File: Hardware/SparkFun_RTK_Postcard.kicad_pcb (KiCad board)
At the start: 4 copper layers, 43.2 x 43.2 mm, 151 parts, among them J1 USB_C_Receptacle, J11 1x10, J2 SMA_Edge, J4 Qwiic_RA, J5 1x09, J6 U.FL, J7 Qwiic_RA, J8 JST_Locking_4, Q1 MBT3904DW1, SW4 Reset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

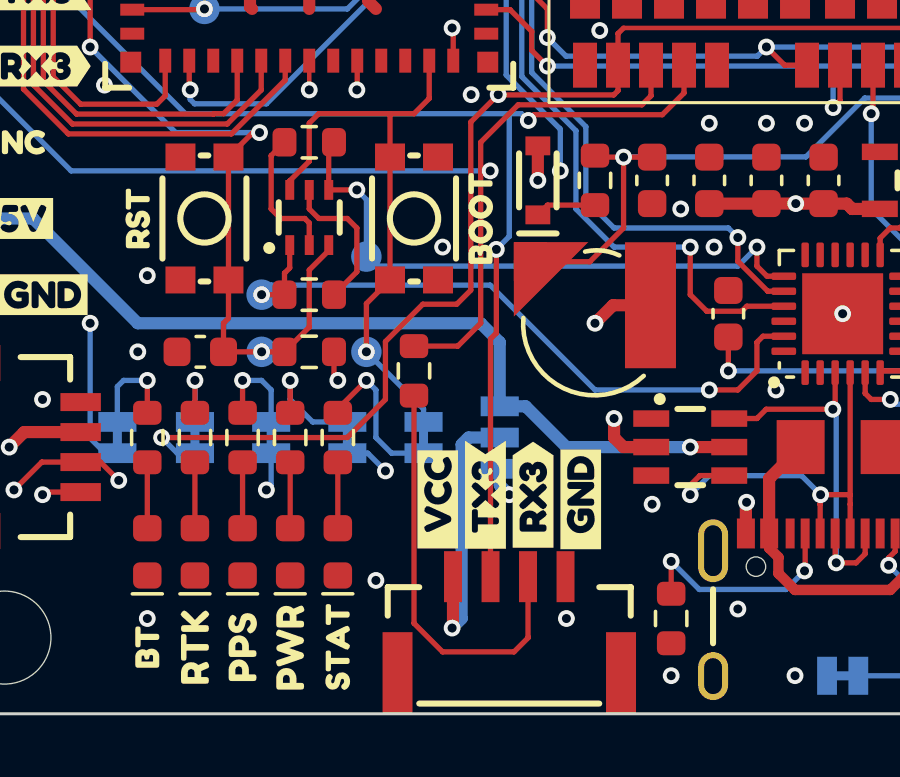
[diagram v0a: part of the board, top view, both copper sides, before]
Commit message: Update to v9 and current libraries.
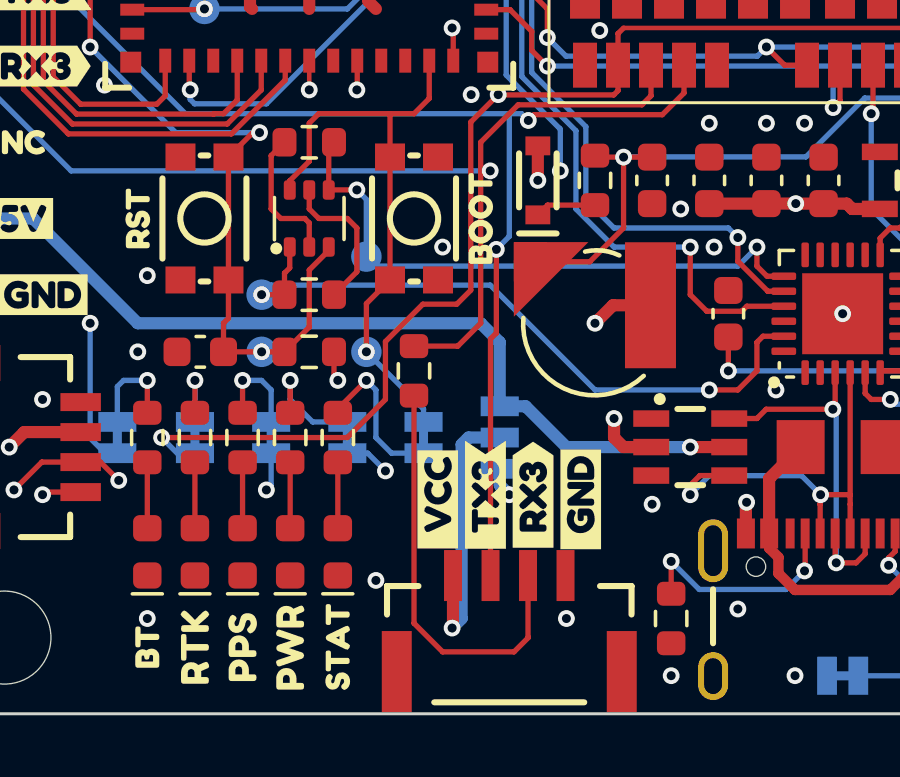
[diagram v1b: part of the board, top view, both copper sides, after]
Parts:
- removed Q1: MBT3904DW1, SparkFun-Semiconductor-Standard:SOT-323
- added Q2: MBT3904DW1, SparkFun-Semiconductor-Standard:SOT-363_SC-70-6, F.Cu at (148.0, 101.0)
- BT1: value 6.8mm_ML414H -> ML414H
- J11: footprint SparkFun-Connector:1x10 -> SparkFun-Connector:1x10_P2.54mm
- J2: footprint SparkFun-Connector:SMA_Edge -> SparkFun-Connector:SMA_Edge_8mm
- J4, J7: footprint SparkFun-Connector:JST_SMD_1.0mm-4_RA -> SparkFun-Connector:JST_1x04_P1.0mm_Horizontal_SMD
- J5: footprint SparkFun-Connector:1x09 -> SparkFun-Connector:1x09_P2.54mm
- J8: footprint SparkFun-Connector:JST_SMD_1.25mm-4_Locking -> SparkFun-Connector:JST_1x04_P1.25mm_Locking_Horizontal_SMD
- JP1: value BT -> ~
- JP2: value PWR -> ~
- JP3: value PPS -> ~
- JP4: value VSEL -> ~
- JP5: value RTK -> ~
- JP6: value I²C-EXT -> ~
- JP7: value SHLD -> ~
- JP8: value STAT -> ~
- SW4: value Reset -> SMD_4.6x2.8mm_h2.5mm
- SW5: value Boot -> SMD_4.6x2.8mm_h2.5mm
- TP1, TP2, TP3, TP4, TP6: value PTH -> 1.0mm
- U3: footprint LG290P:Quectel_LG290P -> SparkFun-GNSS:Quectel_LG290P
- moved J8 1.59 mm to (154.6, 114.6)

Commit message: Add MFi. Update symbols. Use main library sym/fps.
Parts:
- removed Q2: MBT3904DW1, SparkFun-Semiconductor-Standard:SOT-363_SC-70-6
- removed R19, R20: 0, SparkFun-Resistor:R_0402_1005Metric
- added C14: 0.1uF, SparkFun-Capacitor:C_0603_1608Metric, F.Cu at (150.5, 105.1)
- added JP10: ~, SparkFun-Jumper:Jumper_2_NO, F.Cu at (168.3, 81.9)
- added JP9: ~, SparkFun-Jumper:Jumper_2_NC_Trace, F.Cu at (165.7, 80.6)
- added Q1: MBT3904DW1, SparkFun-Semiconductor-Standard:SOT-363_SC-70-6, F.Cu at (148.0, 101.0)
- added U6: MFI343S00177, SparkFun-Semiconductor-Standard:DFN-8_3x2mm_P0.5mm_EP1.66x1.5mm, F.Cu at (153.0, 106.0)
- JP4: value ~ -> VCC
- JP6: value ~ -> I2C
- SW4: value SMD_4.6x2.8mm_h2.5mm -> RESET
- SW5: value SMD_4.6x2.8mm_h2.5mm -> BOOT
- moved R8 2.42 mm to (150.5, 108.3)
- moved J6 0.95 mm to (171.8, 81.9)
- moved C6 0.63 mm to (161.0, 82.2)
- moved D3 0.63 mm to (163.8, 81.6)
- moved L1 0.63 mm to (162.6, 81.6)
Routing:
- net SDA_0: track 29.1 -> 42.2 mm, vias 3 -> 4
- net SCL_0: track 27.4 -> 39.6 mm, vias 2 -> 3
- net GND: track 205.5 -> 209.8 mm
- net 3.3V: track 37.3 -> 40.3 mm, vias 12 -> 14
- net Net-(D3-A2): track 4.88 -> 7.30 mm
- net LG-RXD3: track 35.1 -> 37.3 mm, vias 1 -> 2
- net Net-(J8-Pin_3): track 14.0 -> 12.2 mm
- net Net-(JP8-A): track 5.00 -> 6.52 mm
- net LG-RTK: track 64.8 -> 65.9 mm
- net LG-TXD3: track 42.9 -> 43.9 mm
- net Net-(J6-In): track 2.41 -> 1.56 mm
- net 5V: track 49.8 -> 50.5 mm
- net LG-PPS: track 83.4 -> 84.1 mm
- net Net-(C3-Pad1): track 8.59 -> 7.96 mm
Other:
- board text added: "v11"
- board text removed: "v10"
